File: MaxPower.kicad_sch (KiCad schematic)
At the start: 40 parts, among them J1 Battery, J2 +5 +3.3 GND, SW1 SW_DPDT_x2, U1 LTC3130EMSE, U2 AMS1117-3.3

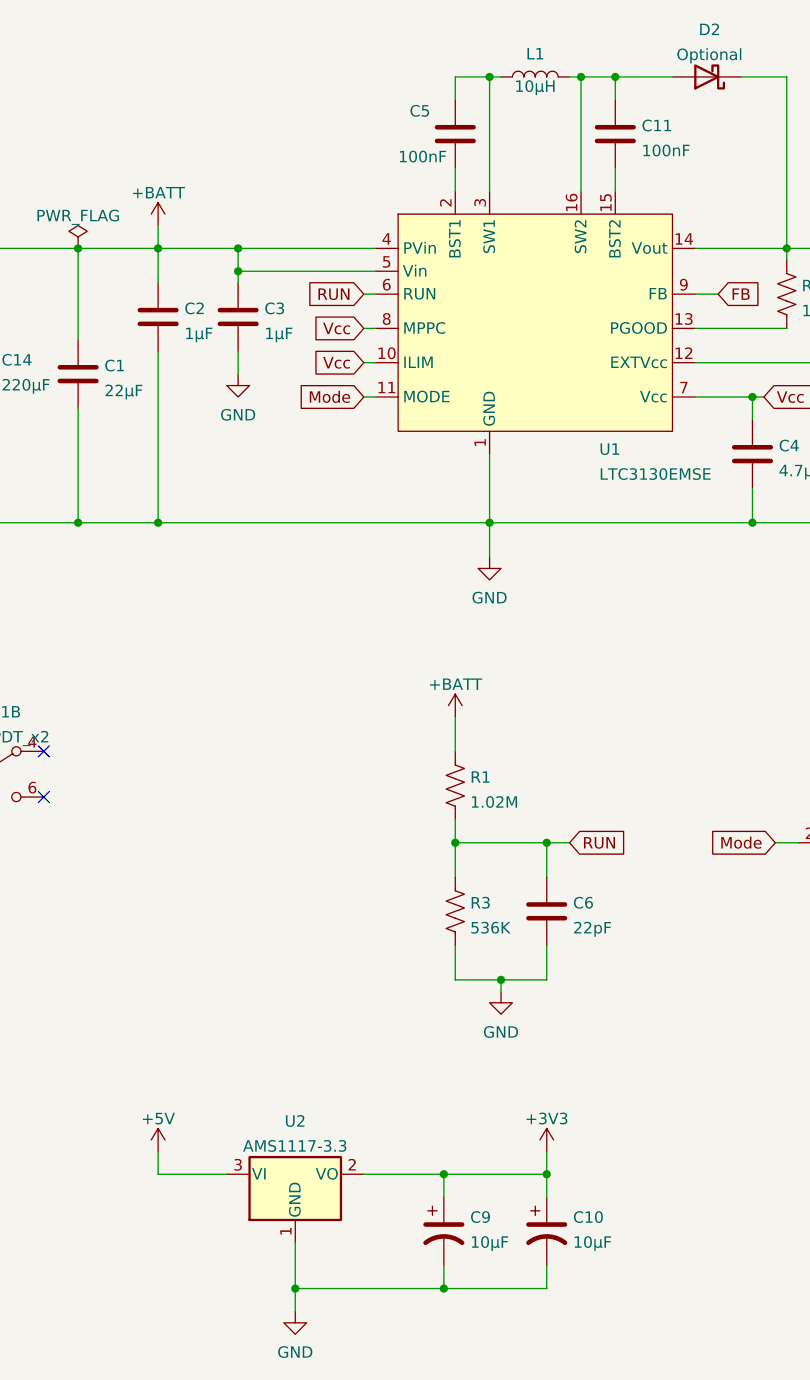
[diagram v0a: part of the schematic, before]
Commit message: Update to kicad 7. Add CC license to drawing.
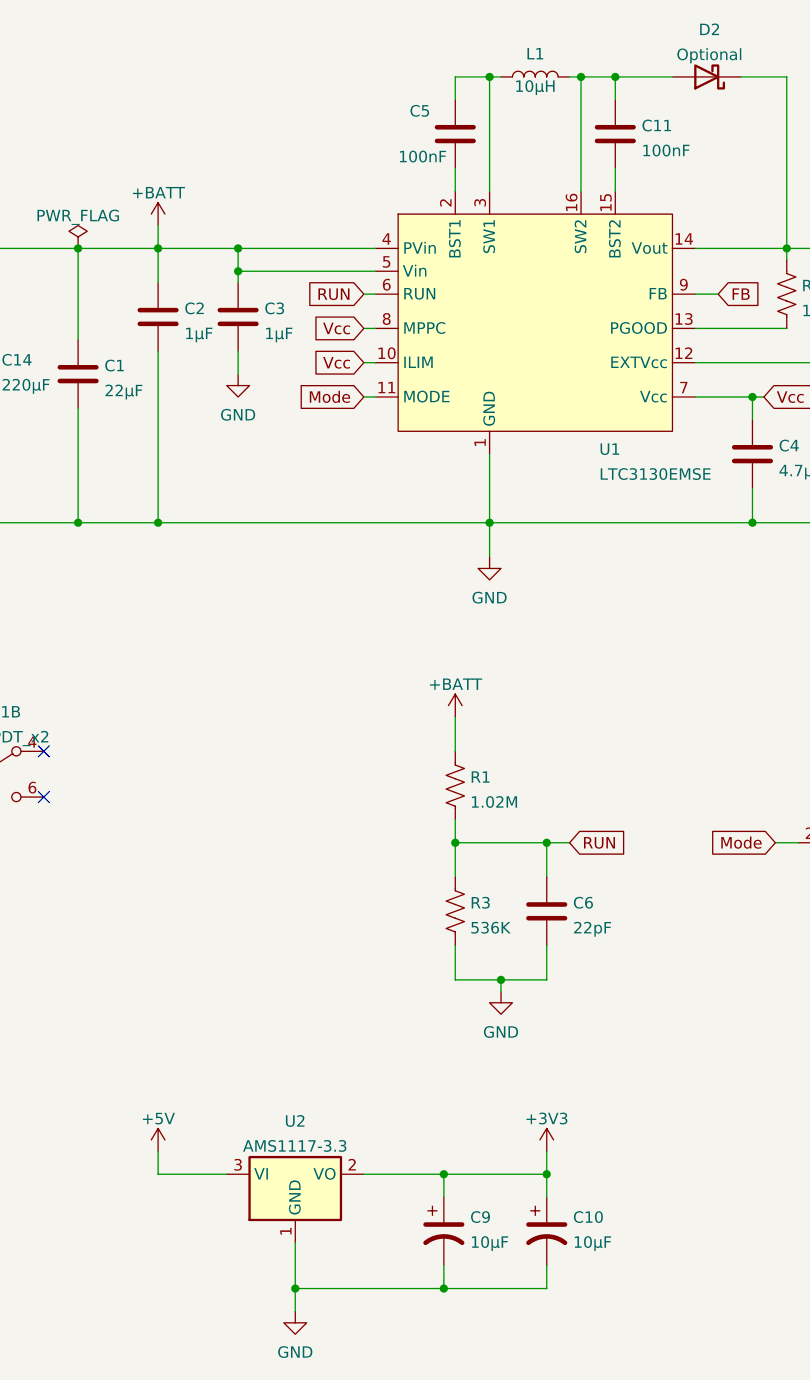
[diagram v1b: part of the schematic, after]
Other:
- title: (none) -> MaxPower

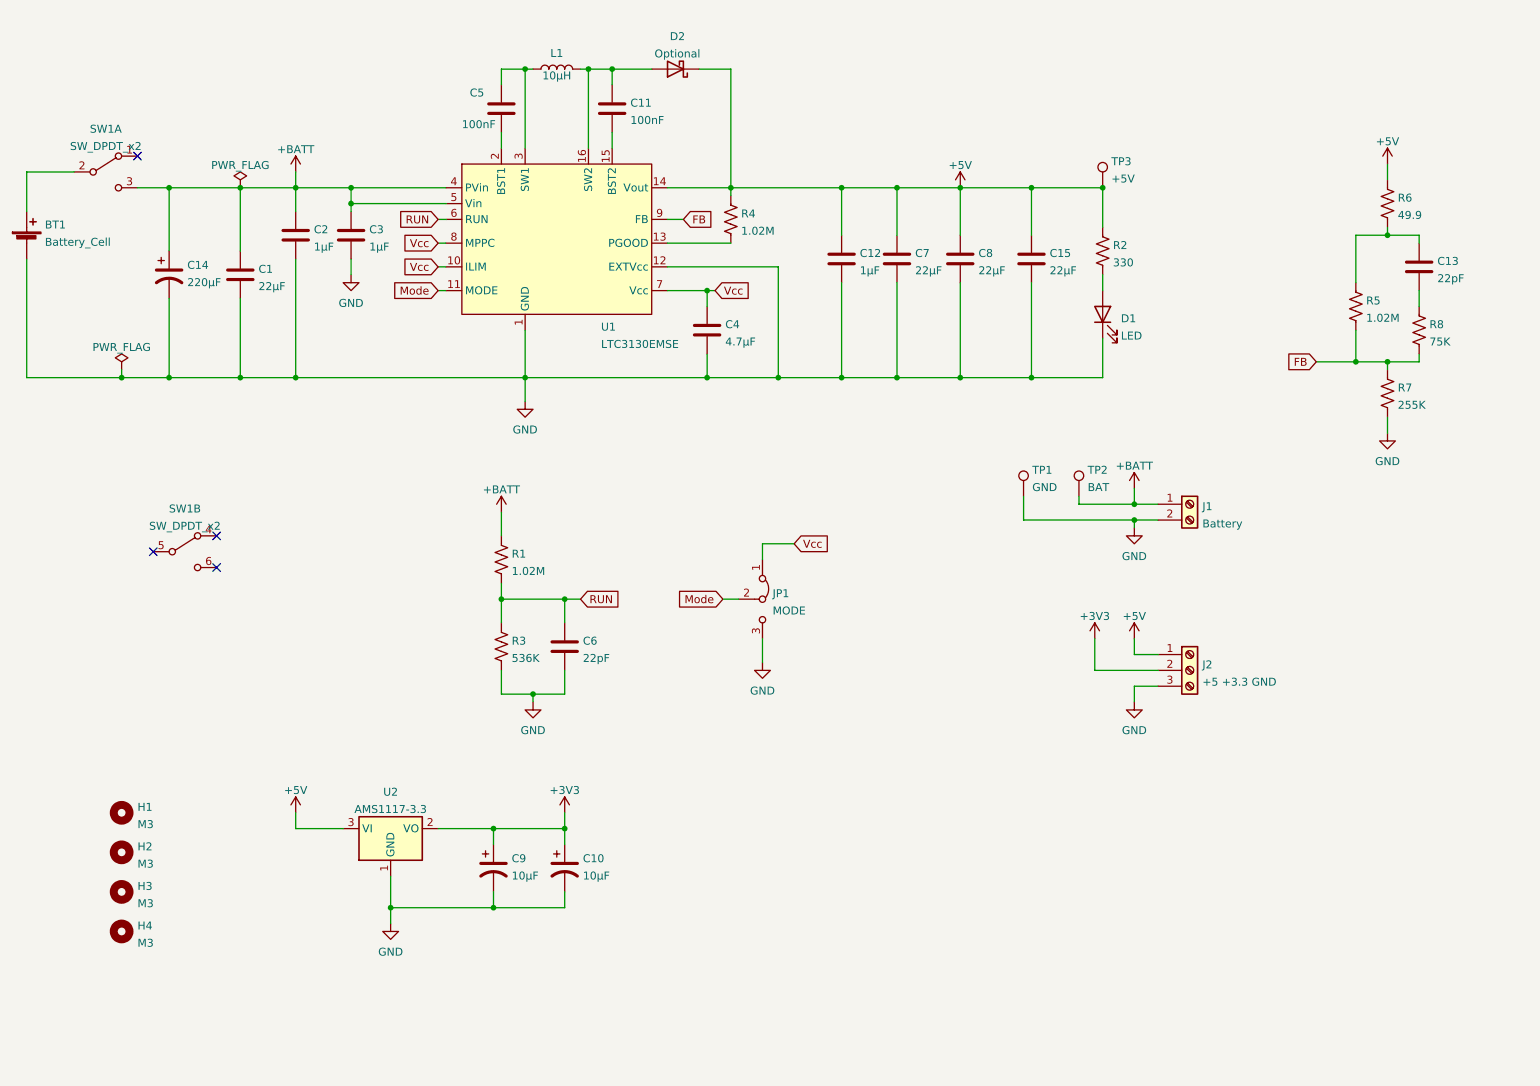
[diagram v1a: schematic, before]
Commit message: Add TP4056 battery charger to schematic and README
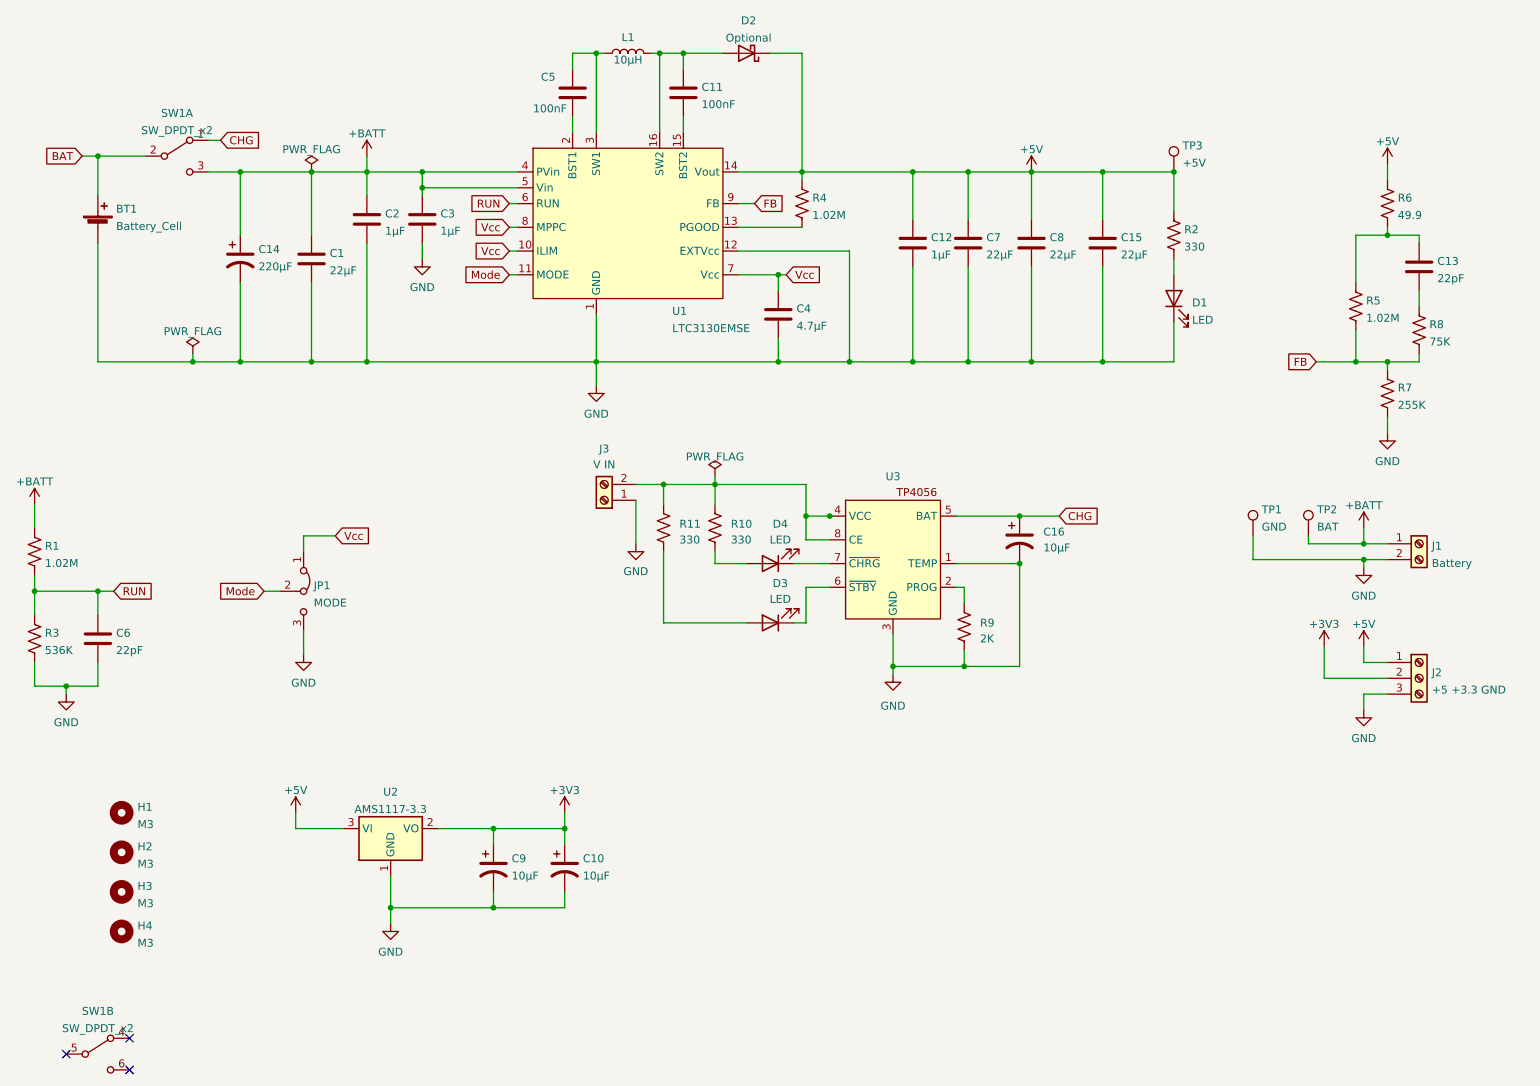
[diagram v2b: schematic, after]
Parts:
- added C16: 10µF, Capacitor_Tantalum_SMD:CP_EIA-3216-18_Kemet-A, symbol Device:C_Polarized_US
- added D3, D4: LED, LED_THT:LED_D3.0mm, symbol Device:LED
- added J3: V IN, TerminalBlock_Phoenix:TerminalBlock_Phoenix_MKDS-1,5-2_1x02_P5.00mm_Horizontal, symbol Connector:Screw_Terminal_01x02
- added R10, R11: 330, Resistor_SMD:R_0805_2012Metric, symbol Device:R_US
- added R9: 2K, symbol Device:R_US
- added U3: ~, symbol TP4056:TP4056-42-ESOP8
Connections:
- net GND: now also C16.2, J3.1 (Pin_1), R9.2, U3.1 (TEMP), U3.3 (GND)
- net BAT: now reaches BT1.1 (+), SW1.2 (B)
- net CHG: now reaches SW1.1 (A)
- net CHG: now also C16.1, U3.5 (BAT)
- new net: D3.1 (K), U3.6 (~{STBY})
- new net: D3.2 (A), R11.2
- new net: D4.2 (A), R10.1
- new net: J3.2 (Pin_2), R10.2, R11.1, U3.4 (VCC), U3.8 (CE)
- new net: R9.1, U3.2 (PROG)
- new net: D4.1 (K), U3.7 (~{CHRG})
- no-connect marks 4 -> 3
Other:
- moved on the sheet: BT1, C1, C11, C12, C14, C15, C2, C3, C4, C5, C6, C7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

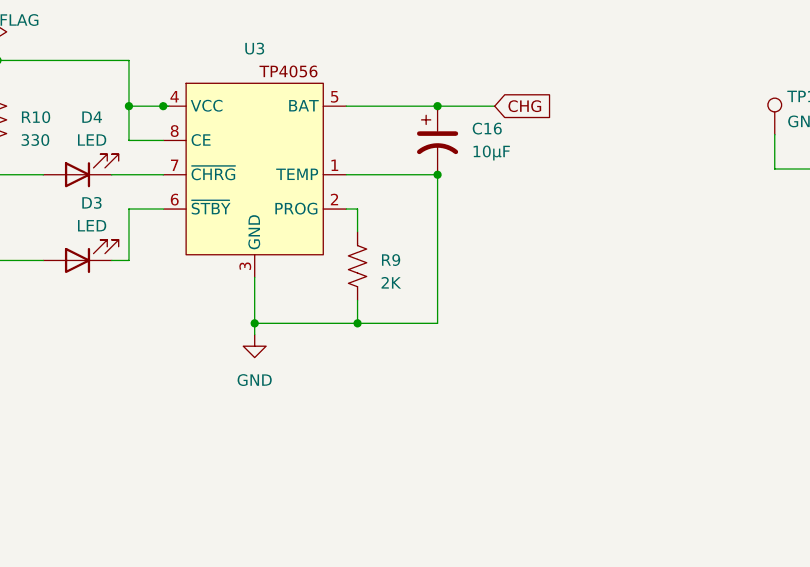
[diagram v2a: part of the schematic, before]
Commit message: Add footprint and LCSC part numbers.
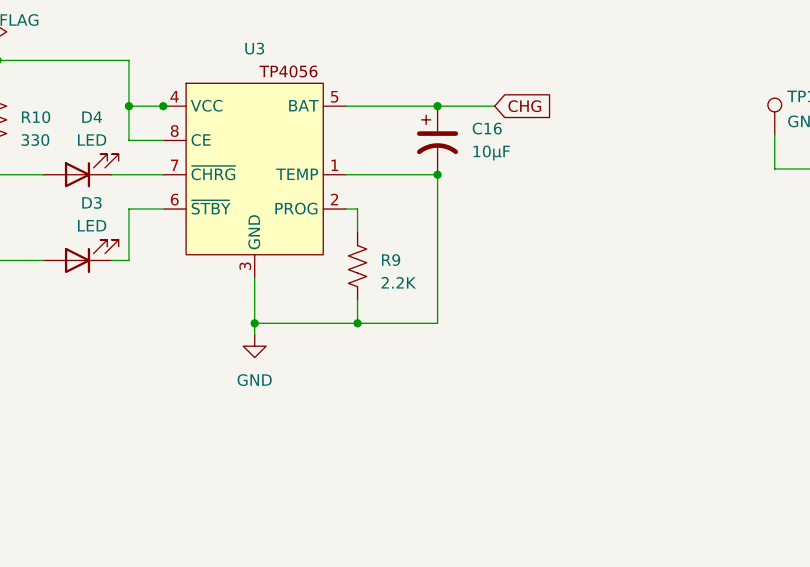
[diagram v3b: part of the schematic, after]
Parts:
- R9: value 2K -> 2.2K; footprint (none) -> Resistor_SMD:R_0805_2012Metric; LCSC (none) -> C17520
- U3: footprint (none) -> Package_SO:Texas_HSOP-8-1EP_3.9x4.9mm_P1.27mm_ThermalVias; LCSC (none) -> C16581
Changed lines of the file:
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@@
       (effects (font (size 1.27 1.27)))
     )
-    (property "Footprint" "" (at 161.925 93.345 0)
+    (property "Footprint" "Package_SO:Texas_HSOP-8-1EP_3.9x4.9mm_P1.27mm_ThermalVias" (at 161.925 93.345 0)
       (effects (font (size 1.27 1.27)) hide)
     )
     (property "Datasheet" "" (at 161.925 93.345 0)
+      (effects (font (size 1.27 1.27)) hide)
+    )
+    (property "LCSC" "C16581" (at 161.925 93.345 0)
       (effects (font (size 1.27 1.27)) hide)
     )
@@
       (effects (font (size 1.27 1.27)) (justify left))
     )
-    (property "Value" "2K" (at 175.895 116.84 0)
-      (effects (font (size 1.27 1.27)) (justify left))
-    )
-    (property "Footprint" "" (at 174.371 115.189 90)
+    (property "Value" "2.2K" (at 175.895 116.84 0)
+      (effects (font (size 1.27 1.27)) (justify left))
+    )
+    (property "Footprint" "Resistor_SMD:R_0805_2012Metric" (at 174.371 115.189 90)
       (effects (font (size 1.27 1.27)) hide)
     )
@@
       (effects (font (size 1.27 1.27)) hide)
     )
+    (property "LCSC" "C17520" (at 173.355 114.935 0)
+      (effects (font (size 1.27 1.27)) hide)
+    )
